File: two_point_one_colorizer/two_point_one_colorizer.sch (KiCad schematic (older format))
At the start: 30 parts, among them J1 rca, J2 rca, J3 Mini-DIN-4, J4 Barrel_Jack, Q1 2N3904, U1 74HC14, U2 4053, U3 LM317, Y1 Crystal

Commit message: update circuits
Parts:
- R2: value 5k -> 5.1k
- R7: value 1M -> 1m
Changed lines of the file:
@@
 Date "2020-07-30"
 Rev ""
-Comp "designed by rob schafer"
-Comment1 "converted to kicad by cyberboy666"
+Comp "original design by rob schafer"
+Comment1 "modified and converted to kicad by cyberboy666"
 Comment2 ""
 Comment3 ""
@@
 P 2075 4250
 F 0 "R7" H 2145 4296 50  0000 L CNN
-F 1 "1M" H 2145 4205 50  0000 L CNN
+F 1 "1m" H 2145 4205 50  0000 L CNN
 F 2 "Resistor_THT:R_Axial_DIN0207_L6.3mm_D2.5mm_P7.62mm_Horizontal" V 2005 4250 50  0001 C CNN
 F 3 "~" H 2075 4250 50  0001 C CNN
@@
 P 1775 1825
 F 0 "R2" H 1845 1871 50  0000 L CNN
-F 1 "5k" H 1845 1780 50  0000 L CNN
+F 1 "5.1k" H 1845 1780 50  0000 L CNN
 F 2 "Resistor_THT:R_Axial_DIN0207_L6.3mm_D2.5mm_P7.62mm_Horizontal" V 1705 1825 50  0001 C CNN
 F 3 "~" H 1775 1825 50  0001 C CNN

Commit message: revised all boards
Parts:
- added J6: Conn_01x03, Connector_PinHeader_2.54mm:PinHeader_1x03_P2.54mm_Vertical, symbol Connector_Generic:Conn_01x03
- added J7: Conn_02x08_Odd_Even, Connector_PinHeader_2.54mm:PinHeader_2x08_P2.54mm_Vertical, symbol Connector_Generic:Conn_02x08_Odd_Even
- added Y2: Crystal, Crystal:Crystal_HC49-4H_Vertical, symbol Device:Crystal
- J1, J2: footprint lib_fp:RCJ-024 -> lib_fp:tht_vertical_rca
- J3: value Mini-DIN-4 -> mini-din4; footprint lib_fp:MiniDin4-MD-40S -> lib_fp:mini-din-4-vertical_KMDVLX-4S-N-1
- U2: value 4053 -> CD4053
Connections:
- net +5V: now also J7.11 (Pin_11), J7.12 (Pin_12)
- net GND: now also J7.3 (Pin_3), J7.4 (Pin_4), J7.5 (Pin_5), J7.6 (Pin_6), J7.7 (Pin_7), J7.8 (Pin_8)
- net at C1.1, R1.2, U1.1: now also J6.2 (Pin_2); no longer Y1.1
- net at C2.1, R2.2, Y1.2: now also Y2.2
- new net: J6.3 (Pin_3), Y1.1
- new net: J6.1 (Pin_1), Y2.1
- no-connect marks 9 -> 17
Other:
- note added: "pal/ntsc"
- moved on the sheet: C1, C10, C11, C2, C20, C4, C5, C6, C7, C8, C9, J4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

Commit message: working on nexr version for colorizer and inverter
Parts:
- removed J6: Conn_01x03, Connector_PinHeader_2.54mm:PinHeader_1x03_P2.54mm_Vertical, symbol Connector_Generic:Conn_01x03
- removed U1: 74HC14, Package_DIP:DIP-14_W7.62mm_LongPads, symbol 74xx:74HC14
- added SW3: SPDT_slide, lib_fp:spdt_slide_switch_small_tayda, symbol Switch:SW_SPDT
- added U1: 4069, Package_DIP:DIP-14_W7.62mm_LongPads, symbol 4xxx:4069
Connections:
- net +5V: now also U1.14 (VDD)
- net GND: now also U1.7 (VSS)
- net colours/crystal: now also U1.4
- net at C3.2, J2.1 (In), R6.1: now also J3.4; no longer J3.3
- net at Y1.1: now also SW3.1 (A)
- net at C1.1, R1.2: now also SW3.2 (B), U1.1
- net at R1.1, R2.1: now also U1.2, U1.3
- net at Y2.1: now also SW3.3 (C)
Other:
- moved on the sheet: C1, C2, J3, R1, R2, Y1

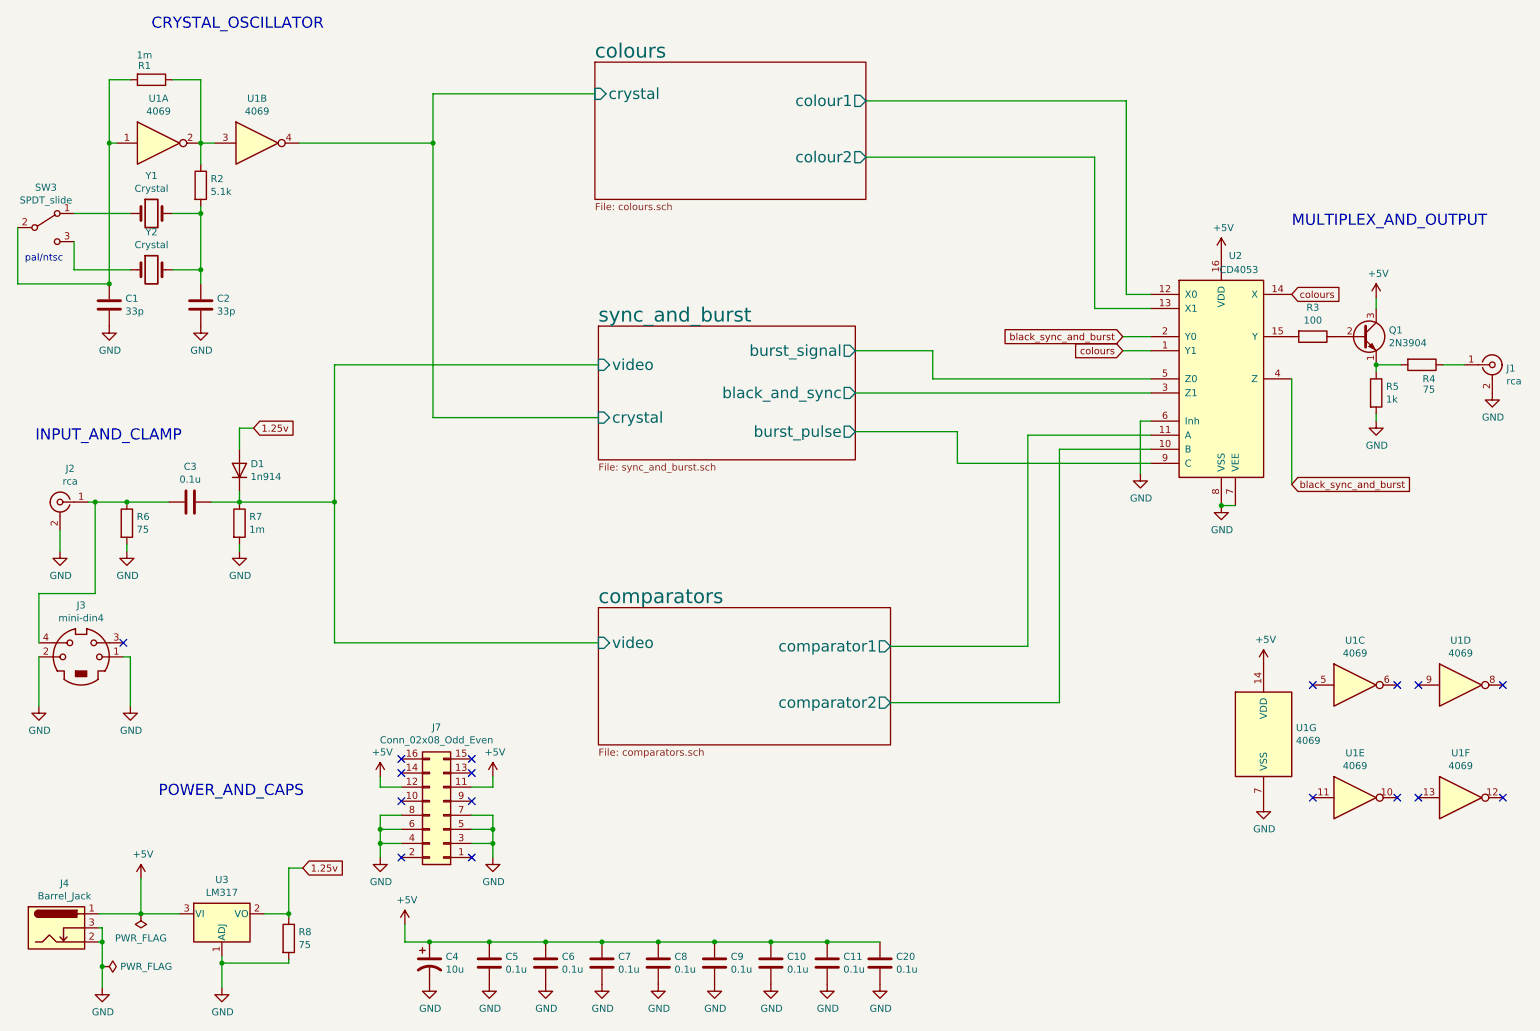
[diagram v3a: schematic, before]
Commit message: lay out colorizer
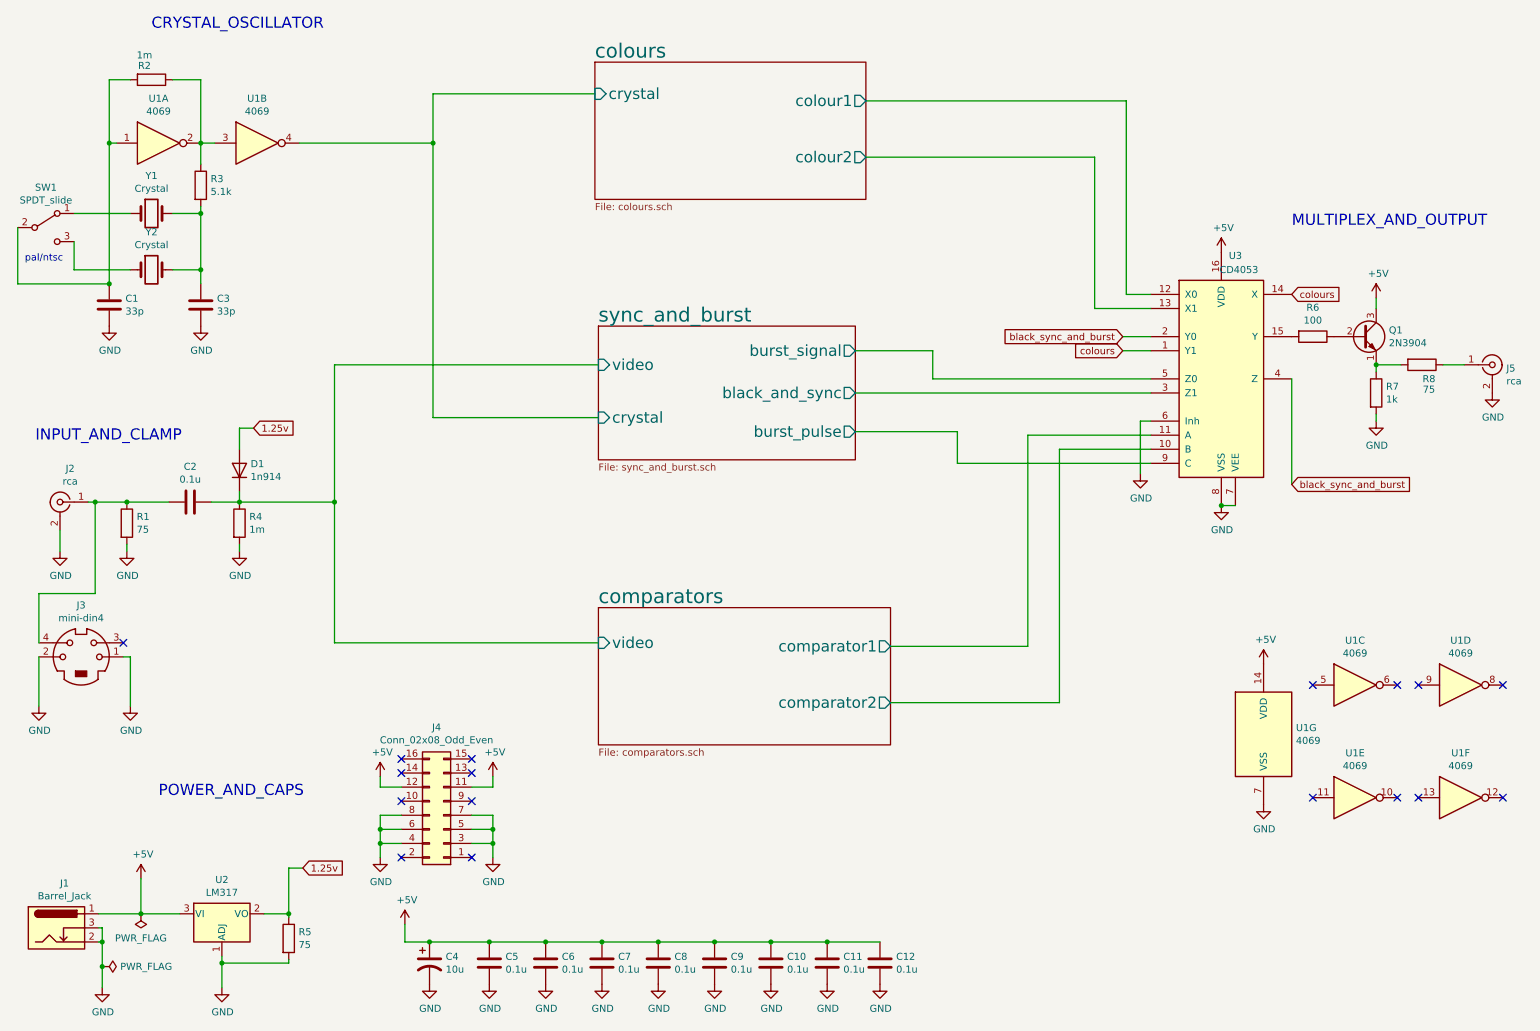
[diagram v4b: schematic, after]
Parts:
- C1, C10, C11, C5, C6, C7, C8, C9: footprint Capacitor_THT:C_Disc_D4.7mm_W2.5mm_P5.00mm -> lib_fp:C_Disc_D4.7mm_W2.5mm_P5.00mm
- C12: renamed from C20; footprint Capacitor_THT:C_Disc_D4.7mm_W2.5mm_P5.00mm -> lib_fp:C_Disc_D4.7mm_W2.5mm_P5.00mm
- C2: renamed from C3; footprint Capacitor_THT:C_Disc_D4.7mm_W2.5mm_P5.00mm -> lib_fp:C_Disc_D4.7mm_W2.5mm_P5.00mm
- C3: renamed from C2; footprint Capacitor_THT:C_Disc_D4.7mm_W2.5mm_P5.00mm -> lib_fp:C_Disc_D4.7mm_W2.5mm_P5.00mm
- R1: renamed from R6; footprint Resistor_THT:R_Axial_DIN0207_L6.3mm_D2.5mm_P7.62mm_Horizontal -> lib_fp:R_Axial_DIN0207_L6.3mm_D2.5mm_P7.62mm_Horizontal
- R2: renamed from R1; footprint Resistor_THT:R_Axial_DIN0207_L6.3mm_D2.5mm_P7.62mm_Horizontal -> lib_fp:R_Axial_DIN0207_L6.3mm_D2.5mm_P7.62mm_Horizontal
- R3: renamed from R2; footprint Resistor_THT:R_Axial_DIN0207_L6.3mm_D2.5mm_P7.62mm_Horizontal -> lib_fp:R_Axial_DIN0207_L6.3mm_D2.5mm_P7.62mm_Horizontal
- R4: renamed from R7; footprint Resistor_THT:R_Axial_DIN0207_L6.3mm_D2.5mm_P7.62mm_Horizontal -> lib_fp:R_Axial_DIN0207_L6.3mm_D2.5mm_P7.62mm_Horizontal
- R5: renamed from R8; footprint Resistor_THT:R_Axial_DIN0207_L6.3mm_D2.5mm_P7.62mm_Horizontal -> lib_fp:R_Axial_DIN0207_L6.3mm_D2.5mm_P7.62mm_Horizontal
- R6: renamed from R3; footprint Resistor_THT:R_Axial_DIN0207_L6.3mm_D2.5mm_P7.62mm_Horizontal -> lib_fp:R_Axial_DIN0207_L6.3mm_D2.5mm_P7.62mm_Horizontal
- R7: renamed from R5; footprint Resistor_THT:R_Axial_DIN0207_L6.3mm_D2.5mm_P7.62mm_Horizontal -> lib_fp:R_Axial_DIN0207_L6.3mm_D2.5mm_P7.62mm_Horizontal
- R8: renamed from R4; footprint Resistor_THT:R_Axial_DIN0207_L6.3mm_D2.5mm_P7.62mm_Horizontal -> lib_fp:R_Axial_DIN0207_L6.3mm_D2.5mm_P7.62mm_Horizontal
- renumbered J4 to J1, J7 to J4, J1 to J5, SW3 to SW1, U3 to U2, U2 to U3

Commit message: newest circuit revisions
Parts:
- Y1: value Crystal -> 3.8MHZ_Crystal
- Y2: value Crystal -> 4.4MHZ_Crystal
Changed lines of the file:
@@
 P 1450 2050
 F 0 "Y1" H 1450 2318 50  0000 C CNN
-F 1 "Crystal" H 1450 2227 50  0000 C CNN
+F 1 "3.8MHZ_Crystal" H 1450 2227 50  0000 C CNN
 F 2 "Crystal:Crystal_HC49-4H_Vertical" H 1450 2050 50  0001 C CNN
 F 3 "~" H 1450 2050 50  0001 C CNN
@@
 P 1450 2450
 F 0 "Y2" H 1450 2718 50  0000 C CNN
-F 1 "Crystal" H 1450 2627 50  0000 C CNN
+F 1 "4.4MHZ_Crystal" H 1450 2627 50  0000 C CNN
 F 2 "Crystal:Crystal_HC49-4H_Vertical" H 1450 2450 50  0001 C CNN
 F 3 "~" H 1450 2450 50  0001 C CNN
